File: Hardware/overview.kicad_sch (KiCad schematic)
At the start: 0 parts

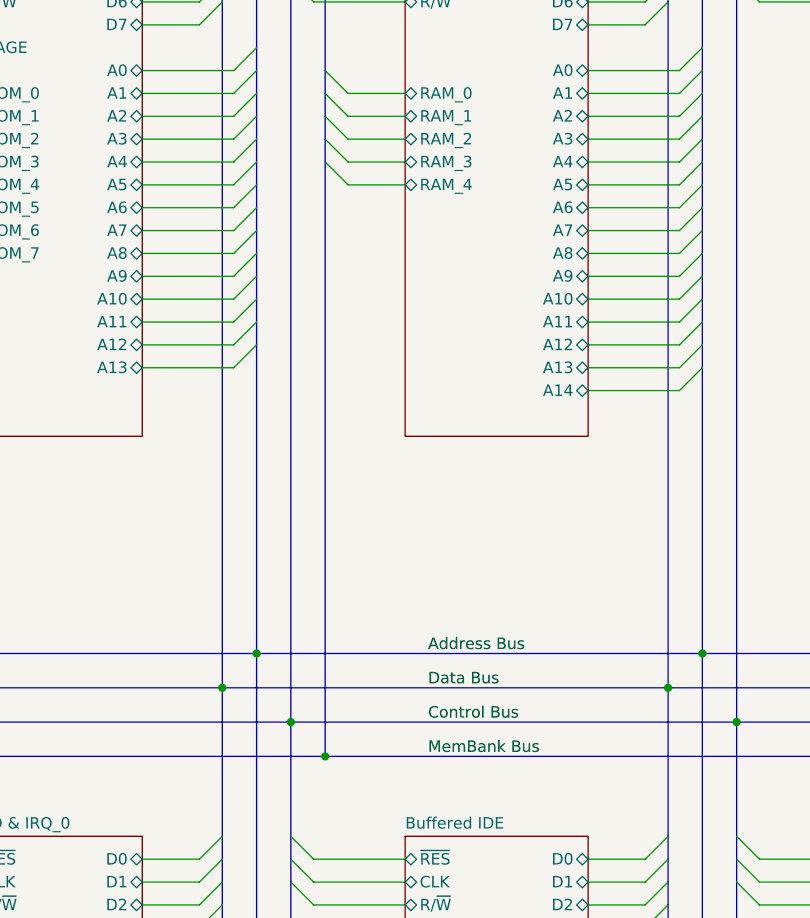
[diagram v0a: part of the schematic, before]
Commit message: Fix mirroring on High-Ram on Bank Select
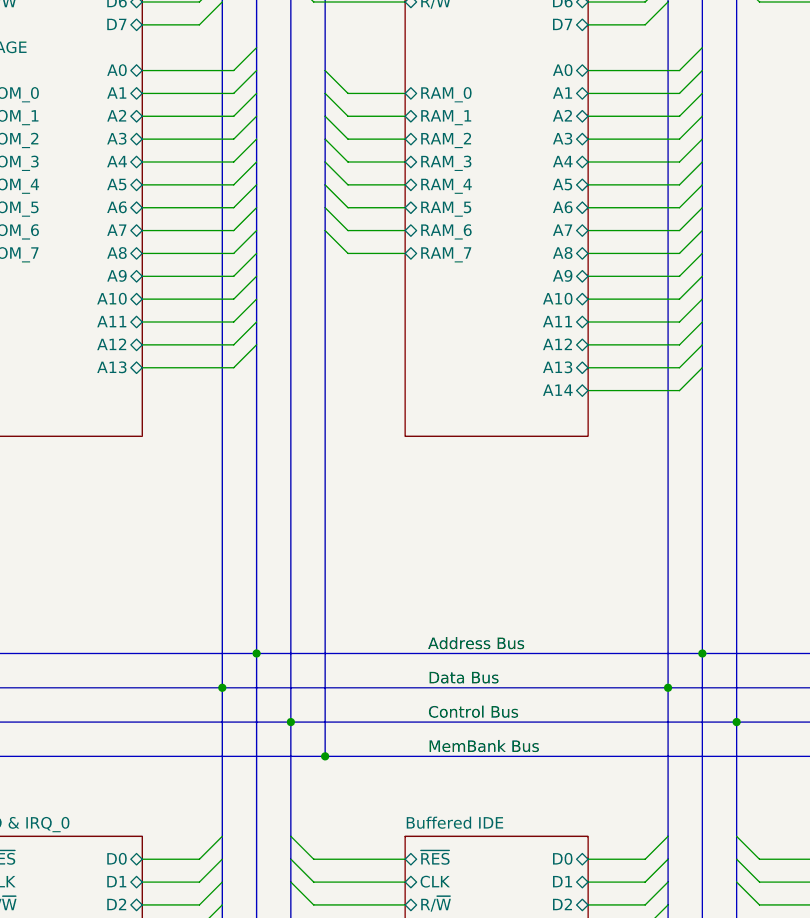
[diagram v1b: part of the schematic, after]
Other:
- sheet RAM ports: added RAM_5, RAM_6, RAM_7; removed none
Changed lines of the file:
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@@
 	)
 	(bus_entry
+		(at 162.56 62.23)
+		(size 2.54 2.54)
+		(stroke
+			(width 0)
+			(type default)
+		)
+	)
+	(bus_entry
 		(at 204.47 231.14)
 		(size -2.54 2.54)
@@
 	)
 	(bus_entry
+		(at 162.56 64.77)
+		(size 2.54 2.54)
+		(stroke
+			(width 0)
+			(type default)
+		)
+	)
+	(bus_entry
 		(at 250.19 214.63)
 		(size -2.54 2.54)
@@
 	)
 	(bus_entry
+		(at 162.56 67.31)
+		(size 2.54 2.54)
+		(stroke
+			(width 0)
+			(type default)
+		)
+	)
+	(bus_entry
 		(at 21.59 217.17)
 		(size -2.54 -2.54)
@@
 	(bus
 		(pts
+			(xy 162.56 64.77) (xy 162.56 67.31)
+		)
+		(stroke
+			(width 0)
+			(type default)
+			(color 221 133 0 1)
+		)
+	)
+	(bus
+		(pts
 			(xy 19.05 77.47) (xy 19.05 80.01)
 		)
@@
 	(wire
 		(pts
+			(xy 165.1 69.85) (xy 171.45 69.85)
+		)
+		(stroke
+			(width 0)
+			(type default)
+		)
+	)
+	(wire
+		(pts
 			(xy 210.82 163.83) (xy 220.98 163.83)
 		)
@@
 	(wire
 		(pts
+			(xy 165.1 67.31) (xy 171.45 67.31)
+		)
+		(stroke
+			(width 0)
+			(type default)
+		)
+	)
+	(wire
+		(pts
 			(xy 290.83 26.67) (xy 297.18 26.67)
 		)
@@
 	(bus
 		(pts
+			(xy 162.56 67.31) (xy 162.56 125.73)
+		)
+		(stroke
+			(width 0)
+			(type default)
+			(color 221 133 0 1)
+		)
+	)
+	(bus
+		(pts
 			(xy 200.66 214.63) (xy 200.66 217.17)
 		)
@@
 		)
 	)
+	(bus
+		(pts
+			(xy 162.56 62.23) (xy 162.56 64.77)
+		)
+		(stroke
+			(width 0)
+			(type default)
+			(color 221 133 0 1)
+		)
+	)
 	(wire
 		(pts
@@
 	(bus
 		(pts
-			(xy 162.56 59.69) (xy 162.56 125.73)
+			(xy 162.56 59.69) (xy 162.56 62.23)
 		)
 		(stroke
@@
 	(wire
 		(pts
+			(xy 165.1 64.77) (xy 171.45 64.77)
+		)
+		(stroke
+			(width 0)
+			(type default)
+		)
+	)
+	(wire
+		(pts
 			(xy 241.3 59.69) (xy 251.46 59.69)
 		)
@@
 			)
 		)
+		(pin "RAM_7" bidirectional
+			(at 171.45 69.85 180)
+			(effects
+				(font
+					(size 1.27 1.27)
+				)
+				(justify left)
+			)
+		)
+		(pin "RAM_5" bidirectional
+			(at 171.45 64.77 180)
+			(effects
+				(font
+					(size 1.27 1.27)
+				)
+				(justify left)
+			)
+		)
+		(pin "RAM_6" bidirectional
+			(at 171.45 67.31 180)
+			(effects
+				(font
+					(size 1.27 1.27)
+				)
+				(justify left)
+			)
+		)
